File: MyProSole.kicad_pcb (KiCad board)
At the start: 2 copper layers, 58.9 x 43.6 mm, 27 parts, among them J1 FSR3, J2 FSR2, J3 FSR3, J4 Conn_01x07_Socket_XIAO_ESP32C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, J5 i2c-bus, J6 SD_CardSocket, J7 XIAO_ESP32C3, J8 SD_CardSocketDummy

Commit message: Removed Old Step
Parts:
- removed the REF** at (81.2, 67.4)
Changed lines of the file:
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@@
 		(embedded_fonts no)
-	)
-	(footprint "MyProSoleLib:ESP32_C3"
-		(layer "F.Cu")
-		(at 81.2 67.4 180)
-		(property "Reference" "REF**"
-			(at 0 -0.5 180)
-			(unlocked yes)
-			(layer "F.SilkS")
-			(effects
-				(font
-					(size 1 1)
-					(thickness 0.1)
-				)
-			)
-		)
-		(property "Value" "ESP32_C3"
-			(at 0 1 180)
-			(unlocked yes)
-			(layer "F.Fab")
-			(effects
-				(font
-					(size 1 1)
-					(thickness 0.15)
-				)
-			)
-		)
-		(property "Datasheet" ""
-			(at 0 0 180)
-			(unlocked yes)
-			(layer "F.Fab")
-			(hide yes)
-			(effects
-				(font
-					(size 1 1)
-					(thickness 0.15)
-				)
-			)
-		)
-		(property "Description" ""
-			(at 0 0 180)
-			(unlocked yes)
-			(layer "F.Fab")
-			(hide yes)
-			(effects
-				(font
-					(size 1 1)
-					(thickness 0.15)
-				)
-			)
-		)
-		(attr smd)
-		(fp_rect
-			(start -15.5 -6.5)
-			(end 5.5 11.5)
-			(stroke
-				(width 0.1)
-				(type default)
-			)
-			(fill no)
-			(layer "F.SilkS")
-		)
-		(fp_text user "${REFERENCE}"
-			(at 0 2.5 180)
-			(unlocked yes)
-			(layer "F.Fab")
-			(effects
-				(font
-					(size 1 1)
-					(thickness 0.15)
-				)
-			)
-		)
-		(embedded_fonts no)
-		(model "/home/bgores/Dokumente/seeed-studio-xiao-esp32-c6-1.snapshot.3/Seeed Studio XIAO ESP32-C6.step"
-			(offset
-				(xyz -7 -8.5 7)
-			)
-			(scale
-				(xyz 1 1 1)
-			)
-			(rotate
-				(xyz -90 -0 -0)
-			)
-		)
 	)
 	(footprint "Diode_SMD:D_SOD-523"

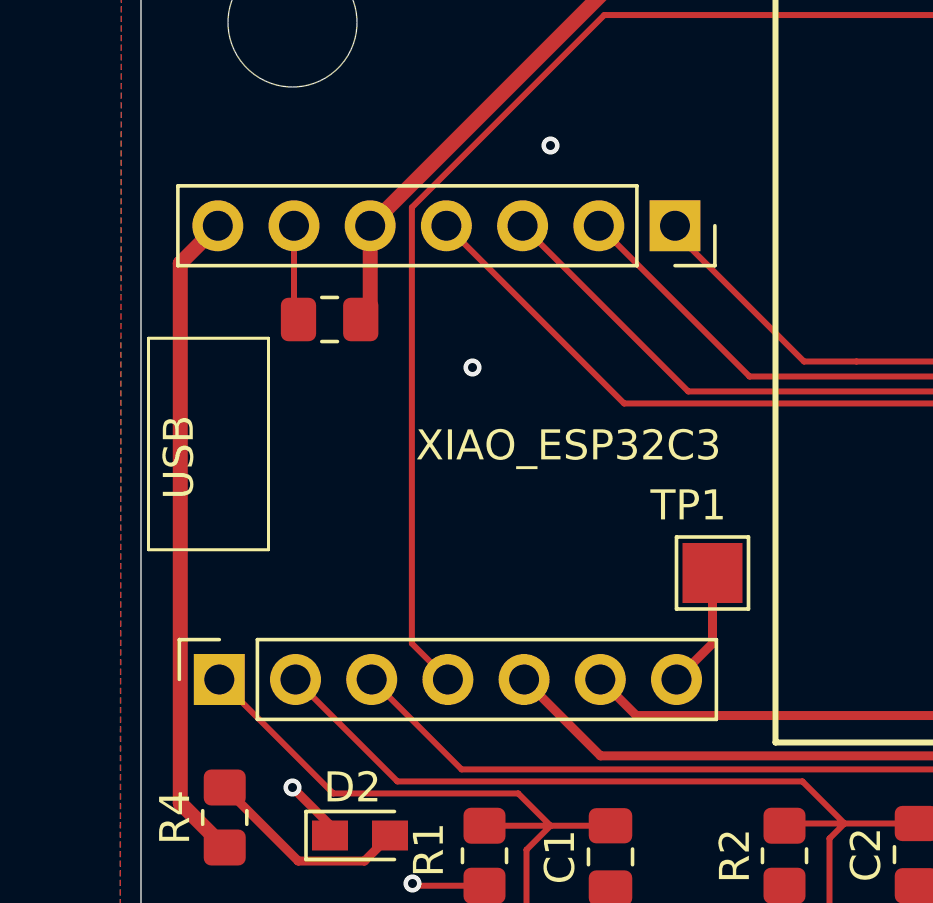
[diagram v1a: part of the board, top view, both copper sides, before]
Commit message: Added ESP for 3dmodel to pcb
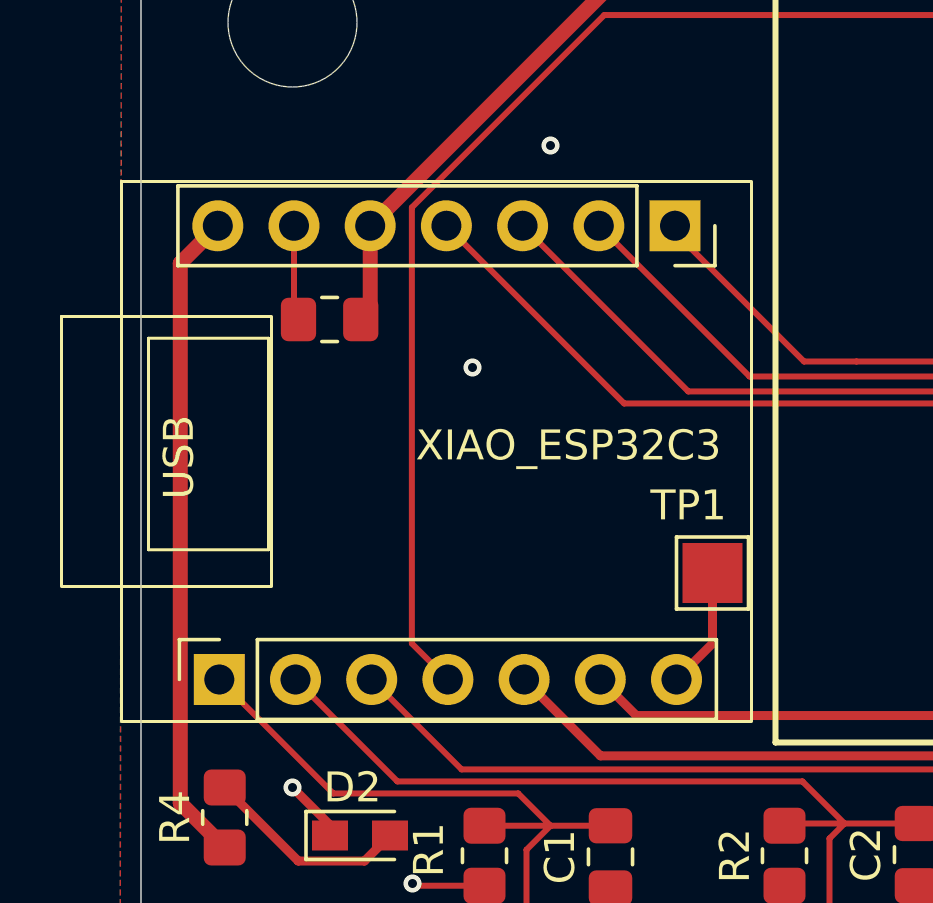
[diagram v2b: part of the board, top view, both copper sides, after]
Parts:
- added REF**: Seeed_ESP32C3_Offset, MyProSoleLibrary:Seeed_ESP32C3_Offset, F.Cu at (86.0, 64.0)
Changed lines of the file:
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@@
+		)
+	)
+	(footprint "MyProSoleLibrary:Seeed_ESP32C3_Offset"
+		(layer "F.Cu")
+		(at 86 64)
+		(property "Reference" "REF**"
+			(at 0 -0.5 0)
+			(unlocked yes)
+			(layer "F.SilkS")
+			(hide yes)
+			(effects
+				(font
+					(size 1 1)
+					(thickness 0.1)
+				)
+			)
+		)
+		(property "Value" "Seeed_ESP32C3_Offset"
+			(at 0 1 0)
+			(unlocked yes)
+			(layer "F.Fab")
+			(hide yes)
+			(effects
+				(font
+					(size 1 1)
+					(thickness 0.15)
+				)
+			)
+		)
+		(property "Datasheet" ""
+			(at 0 0 0)
+			(unlocked yes)
+			(layer "F.Fab")
+			(hide yes)
+			(effects
+				(font
+					(size 1 1)
+					(thickness 0.15)
+				)
+			)
+		)
+		(property "Description" ""
+			(at 0 0 0)
+			(unlocked yes)
+			(layer "F.Fab")
+			(hide yes)
+			(effects
+				(font
+					(size 1 1)
+					(thickness 0.15)
+				)
+			)
+		)
+		(attr smd)
+		(fp_rect
+			(start -12.5 -3.5)
+			(end -5.5 5.5)
+			(stroke
+				(width 0.1)
+				(type default)
+			)
+			(fill no)
+			(layer "F.SilkS")
+		)
+		(fp_rect
+			(start -10.5 -8)
+			(end 10.5 10)
+			(stroke
+				(width 0.1)
+				(type default)
+			)
+			(fill no)
+			(layer "F.SilkS")
+		)
+		(embedded_fonts no)
+		(model "${KIPRJMOD}/step_files/Seeed Studio XIAO-ESP32-C3.step"
+			(offset
+				(xyz 2 5.5 9.5)
+			)
+			(scale
+				(xyz 1 1 1)
+			)
+			(rotate
+				(xyz -90 -0 -180)
+			)
 		)
 	)

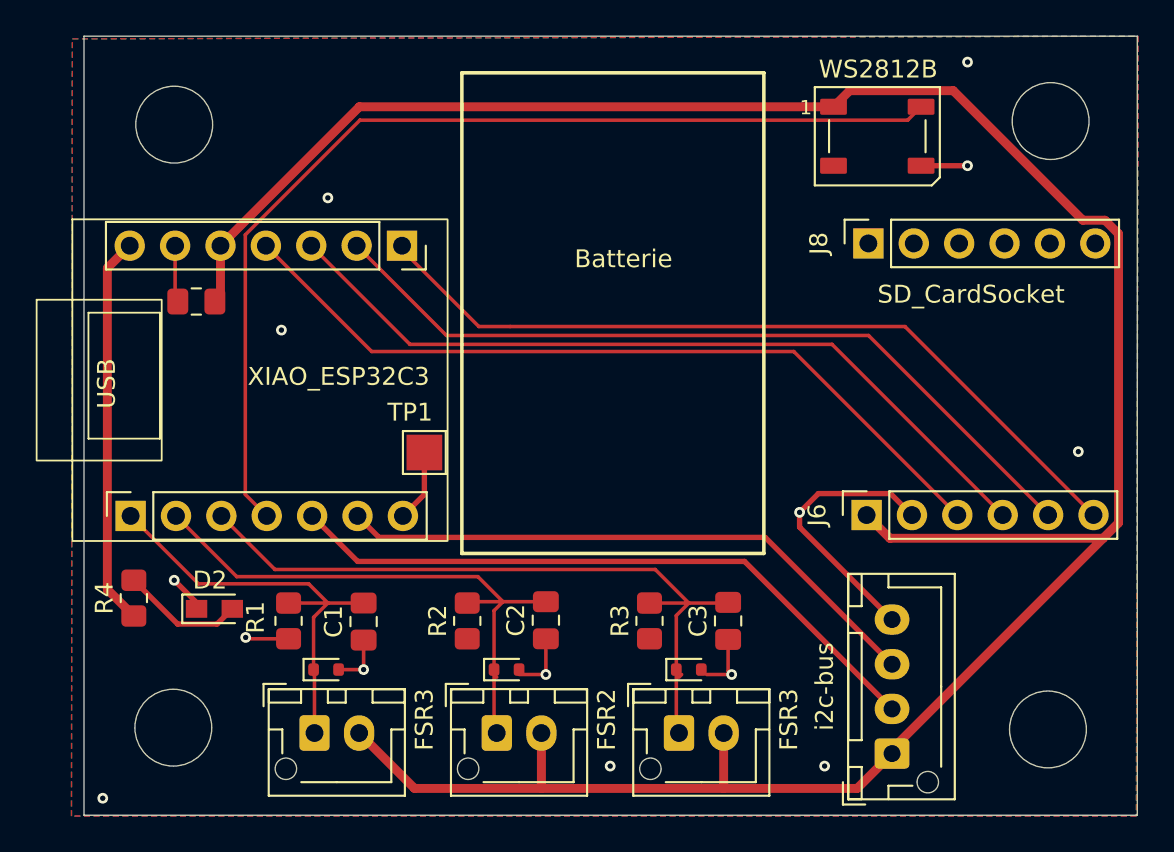
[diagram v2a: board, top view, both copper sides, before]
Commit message: Added all 3d model files
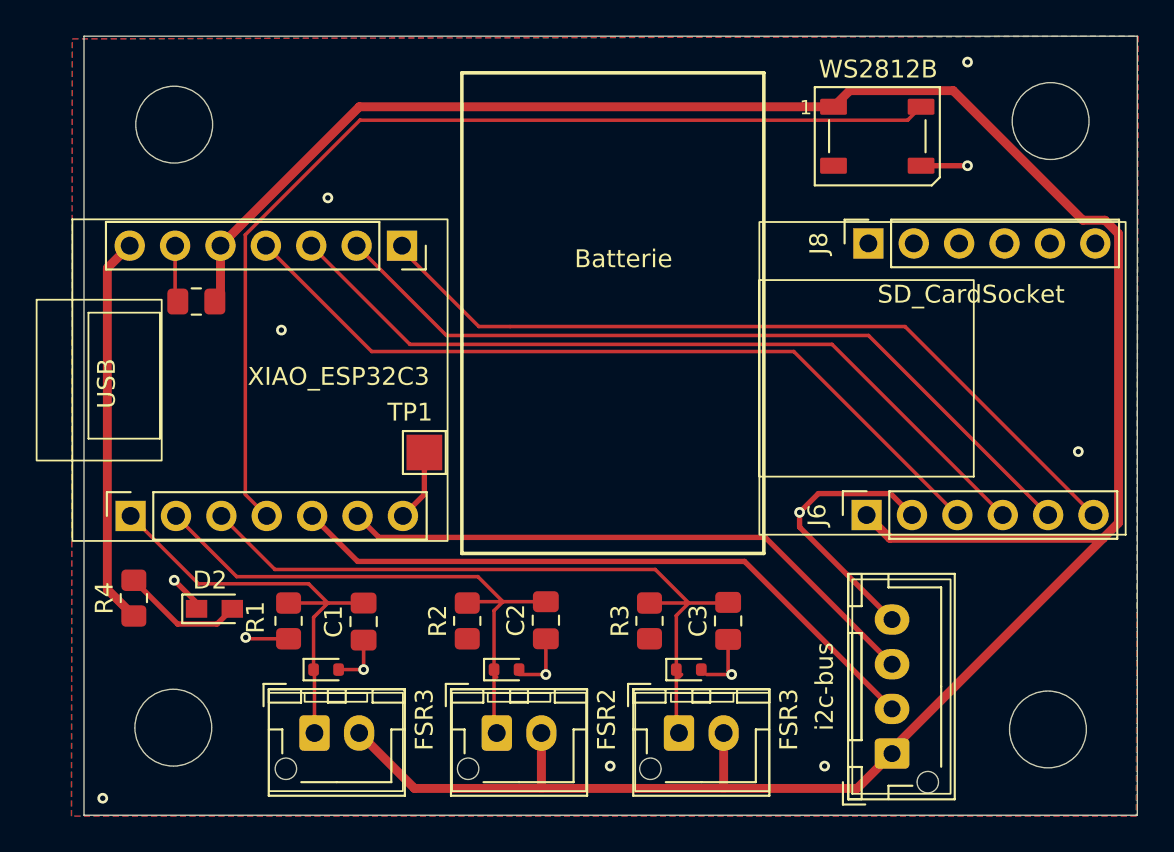
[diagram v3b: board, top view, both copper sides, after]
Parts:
- added REF**: 2pin_jst, MyProSoleLibrary:2pin_jst, F.Cu at (114.5, 85.5)
- added REF**: jst_4pin, MyProSoleLibrary:jst_4pin, F.Cu at (121.9, 82.4)
- added REF**: 2pin_jst, MyProSoleLibrary:2pin_jst, F.Cu at (94.0, 85.5)
- added REF**: 2pin_jst, MyProSoleLibrary:2pin_jst, F.Cu at (104.2, 85.5)
- added REF**: diy_sdcard, MyProSoleLibrary:diy_sdcard, F.Cu at (125.7, 68.7)

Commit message: Version 1.1
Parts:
- removed the REF** at (114.5, 85.5)
- removed the REF** at (94.0, 85.5)
- removed the REF** at (104.2, 85.5)
- added F1: BAT_FUSED, Fuse:Fuse_1206_3216Metric_Pad1.42x1.75mm_HandSolder, F.Cu at (116.8, 47.4)
- added J9: BAT_RAW, Connector_JST:JST_PH_B2B-PH-K_1x02_P2.00mm_Vertical, F.Cu at (116.4, 53.1)
- added REF**: 2pin_jst, MyProSoleLibrary:2pin_jst, F.Cu at (114.5, 85.7)
- added REF**: 2pin_jst, MyProSoleLibrary:2pin_jst, F.Cu at (94.1, 85.5)
- added REF**: 2pin_jst, MyProSoleLibrary:2pin_jst, F.Cu at (104.2, 85.7)
- added SW1: SW_SPDT, MyProSoleLibrary:WS-SLTU THT Mini Slide Switch, F.Cu at (91.2, 51.7)
- added TP2: +, TestPoint:TestPoint_Pad_2.0x2.0mm, F.Cu at (94.8, 69.2)
- added TP3: -, TestPoint:TestPoint_Pad_2.0x2.0mm, F.Cu at (94.8, 65.8)
- D2: value USB-LED -> 5V Power LED
- moved TP1 10.7 mm to (105.7, 71.2)
- moved REF** 8.21 mm to (122.2, 61.2), turned to 0 degrees
- moved D1 2.38 mm to (122.8, 52.0), turned to -90 degrees
- moved REF** 0.35 mm to (86.3, 64.0)
- moved REF** 0.20 mm to (122.1, 82.4)
- moved REF** 0.10 mm to (81.1, 50.7)
- moved J2 0.10 mm to (99.2, 84.8)
- moved J3 0.10 mm to (109.5, 84.8)
- moved J5 0.08 mm to (121.3, 85.9)
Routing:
- net Net-(SW1-B): track 0.00 -> 35.5 mm, vias 0 -> 1
- net Net-(J9-Pin_1): track 0.00 -> 26.9 mm, vias 0 -> 2
- net Net-(SW1-C): track 0.00 -> 24.3 mm, vias 0 -> 1
- net Net-(J4-GPIO_21): track 4.05 -> 12.2 mm
- net Net-(J9-Pin_2): track 0.00 -> 4.15 mm
- net GND: track 35.7 -> 39.6 mm, vias 14 -> 12
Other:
- board text added: "MyProSole V1.10 BG/2026-01"
- board text added: "PWR_ON_SWITCH"
- board text removed: "MyProSole V1.01 BG/2026-01"

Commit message: Last push from Tuxedo
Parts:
- moved REF** 8.57 mm to (126.2, 68.8), turned to 180 degrees
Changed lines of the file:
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@@
 	(footprint "MyProSoleLibrary:diy_sdcard"
 		(layer "F.Cu")
-		(at 122.25 61.2)
+		(at 126.2 68.8 180)
 		(property "Reference" "REF**"
-			(at 0 -0.5 0)
+			(at 0 -0.5 180)
 			(unlocked yes)
 			(layer "F.SilkS")
@@
 		)
 		(property "Value" "diy_sdcard"
-			(at 0 1 0)
+			(at 0 1 180)
 			(unlocked yes)
 			(layer "F.Fab")
@@
 		)
 		(property "Datasheet" ""
-			(at 0 0 0)
+			(at 0 0 180)
 			(unlocked yes)
 			(layer "F.Fab")
@@
 		)
 		(property "Description" ""
-			(at 0 0 0)
+			(at 0 0 180)
 			(unlocked yes)
 			(layer "F.Fab")
@@
 		(attr smd)
 		(fp_rect
-			(start -8.75 -5)
-			(end 11.75 12.5)
+			(start -0.25 -1.75)
+			(end 11.75 9.25)
 			(stroke
 				(width 0.1)
@@
 		)
 		(fp_rect
-			(start -0.25 -1.75)
-			(end 11.75 9.25)
+			(start -8.75 -5)
+			(end 11.75 12.5)
 			(stroke
 				(width 0.1)

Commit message: Swap SD Card GND and 3V3
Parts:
- TP2: value + -> TestPoint
- TP3: value - -> TestPoint
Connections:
- J6 pad 1: +3.3V -> GND
- J6 pad 2: GND -> +3.3V
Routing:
- net GND: track 39.6 -> 36.2 mm
- net +3.3V: track 146.5 -> 143.5 mm
